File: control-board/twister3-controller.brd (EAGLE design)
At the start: 275.6 x 100 mm, 47 parts, among them IC2 TMC2130-LA, U1 MAX6816, U2 LCD-16X2SILK, U3 IS31FL3193, U4 MIC4680-5.0YM-TR

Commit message: Pretty much done with r1.0 of control board
- Stacking PCB design
- Top PCB is a panel that fits into a plastic enclosure
- Bottom holds electronics (Teensy 3.2, LCD, motor driver, encoder, etc)
- 0.1" headers hold the two boards together
- I'm trying to use hacked GND press clips to clip the LCD PCB to the
panel board instead of screws/standoffs. The goal is the two PCBs should
snap together without screws.
- I ordered the DK parts to check fits etc. I will then make final
changes and send out PCB.
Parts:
- removed CFG1, CFG2: JUMPER3-0201, we-rcl:JUMPER3-0201
- removed IC2: TMC2130-LA, we-chip:QFN36-PAD
- removed JP10, JP8, JP9: (no value), pinhead:1X01
- removed R20: 20k, we-rcl:POT_EVM3R
- removed SPI1: JUMPER2-0402-NC, we-rcl:JUMPER2-0402_NC
- removed U$1: TEENSY_3.1_ALL_PINS_AND_PADS, jonnew:TEENSY_3.1_ALLPINS
- added J10, J12, J8, J9: (no value), jonnew:1X04
- added J11, J3, J4, J5, J6: (no value), jonnew:JP4_SMD
- added J2: OSTVN04A150, jonnew:1X04
- added J7: BARREL-JACK_PJ-063BH, jonnew:PJ-063BH
- added R10: 20k, jonnew:SM-42/43W
- added R12: 4.7k, jonnew:0805
- added R14, R15: 4.7k, cyclops:0603
- added R16: 100k, jonnew:0805
- added S2: 800AWSP9M2QE, jonnew:800AWSP9M2QE
- added TP1: RESET, jonnew:TESTPOINT_1MM
- added TP2, TP3, TP4: S7121-42R, jonnew:S7121-42R
- added U10: Teensy 3.2, jonnew:TEENSY_3.1_CYCLOPS
- added U11: TMC2130-LA, we-chip:QFN36-PAD
- C12: device rcl:C0603 -> jonnew:0603
- C13, C16, C17, R22: device we-rcl:C0402 -> jonnew:0402
- C14: value 470n/10V -> 470nF/10V; device we-rcl:C0402 -> jonnew:0402
- C15: value 4u7/10V -> 47uF/10V; device we-rcl:C0402 -> jonnew:0402
- C18: value 100n/50V -> 100nF/50V; device we-rcl:C0402 -> jonnew:0402
- C19: value 22n/50V -> 22nF/50V; device we-rcl:C0402 -> jonnew:0402
- J1: device jonnew:SCREW4 -> jonnew:1X04
- R18, R19: value R0805/0R11 -> 0.11; device rcl:M0805 -> jonnew:0805
- R2: value (none) -> 20k
- R23: value 2R2 -> 2.2; device we-rcl:C0402 -> jonnew:0402
- S1: value (none) -> EC12P
- U2: value LCD-16X2SILK -> GDM1602K
- U4: device jonnew:SOP65P490X110-8N -> jonnew:SOIC127P500X400-8N
- moved C8 258.5 mm to (89.6, 34.2), flipped to the bottom, turned to 270 degrees
- moved C7 226.3 mm to (70.8, 30.2), flipped to the bottom, turned to 270 degrees
- moved D1 225.0 mm to (76.5, 34.5), flipped to the bottom, turned to 90 degrees
- moved U4 220.9 mm to (81.6, 33.3), flipped to the bottom, turned to 270 degrees
- moved L1 215.8 mm to (72.7, 44.6), flipped to the bottom, turned to 180 degrees
- moved C1 198.6 mm to (66.1, 21.6), flipped to the bottom
- moved C6 190.0 mm to (55.6, 20.0), flipped to the bottom, turned to 90 degrees
- moved C5 186.6 mm to (53.3, 20.0), flipped to the bottom, turned to 90 degrees
- moved U3 181.2 mm to (49.9, 18.1), flipped to the bottom
- moved R7 181.0 mm to (44.4, 16.2), flipped to the bottom, turned to 180 degrees
- moved R3 180.0 mm to (44.4, 18.6), flipped to the bottom, turned to 180 degrees
- moved R19 173.3 mm to (60.6, 38.7), flipped to the bottom, turned to 0 degrees
- moved JP6 170.1 mm to (53.0, 33.7), flipped to the bottom, turned to 0 degrees
- moved C16 170.1 mm to (60.4, 41.3), flipped to the bottom
- moved C12 169.5 mm to (62.1, 43.3), flipped to the bottom, turned to 90 degrees
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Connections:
- net N$5 renamed SW
- removed net !SHDN: U3.1
- removed net +5V: C15.2, IC2.25, R22.2, R23.2
- removed net AREF: U$1.AREF
- removed net CFG-0: IC2.5, JP6.4
- removed net CFG-1: IC2.4, JP6.7
- removed net CFG-2: IC2.3, JP6.6
- removed net CFG-3: IC2.2, JP6.5
- removed net MISO: U$1.12
- removed net MOSI: U$1.11
- removed net N$12: U$1.0, U2.4
- removed net N$13: U$1.1, U2.5
- removed net N$14: U$1.2, U2.6
- removed net N$15: U$1.3, U2.7
- removed net N$16: U$1.4, U2.8
- removed net N$17: U$1.5, U2.9
- removed net N$18: U$1.6, U2.10
- removed net N$19: U$1.7, U2.11
- removed net N$20: U$1.8, U2.12
- removed net N$21: U$1.9, U2.13
- removed net N$22: U$1.10, U2.14
- removed net N$30: IC2.10, SPI1.2
- removed net SCLK: U$1.13
- removed net VBAT: U$1.VBAT
- removed net VIO: C13.2, CFG1.3, CFG2.3, IC2.8, JP7.7
- removed net VUSB: U$1.VUSB
- new net !IS31_SHDN: R16.1, U10.33, U3.1
- new net +5VOUT: C15.2, R22.2, R23.2, U11.25
- new net CFG-0/MISO: JP6.4, U10.12, U11.5
- new net CFG-1/MOSI: JP6.7, U10.11, U11.4
- new net CFG-2/SCLK: JP6.6, U10.13, U11.3
- new net CFG-3/!TMC_CS: JP6.5, U10.31, U11.2
- new net DB0: U10.3, U2.7
- new net DB1: U10.4, U2.8
- new net DB2: U10.5, U2.9
- new net DB3: U10.6, U2.10
- new net DB4: U10.7, U2.11
- new net DB5: U10.8, U2.12
- new net DB6: U10.9, U2.13
- new net DB7: U10.10, U2.14
- new net E: U10.2, U2.6
- new net MECH1: J11.1, J11.2, J11.3, J11.4
- new net MECH2: J6.1, J6.2, J6.3, J6.4
- new net MECH3: J4.1, J4.2, J4.3, J4.4, TP2.P$1
- new net MECH4: J5.1, J5.2, J5.3, J5.4, TP3.P$1, TP4.P$1
- new net N$23: S2.1, TP1.1
- new net N$6: J2.1, J3.4
- new net N$7: J2.2, J3.3
- new net N$8: J2.3, J3.2
- new net N$9: J2.4, J3.1
- new net RS: U10.0, U2.4
- new net RW: U10.1, U2.5
- new net SD_MODE: U10.16/A2, U11.9
- new net SPI_MODE: U10.15/A1, U11.10
- net +24V0: now also J7.1, U11.16, U11.30, U11.31; no longer IC2.16, IC2.30, IC2.31
- net +3V3: now also C13.2, JP7.7, U10.3.3V, U10.3.3V2, U11.8; no longer R1.2, R2.1, R3.1, R6.2, R7.1, U$1.3.3V, U$1.3.3V1, U$1.3.3V2, U2.15, U2.2
- net +5V0: now also R1.2, R12.2, R14.2, R15.2, R2.1, R3.1, R6.2, R7.1, U10.VIN, U2.15, U2.2; no longer U$1.VIN
- net AGND: now also U10.AGND; no longer U$1.AGND
- net BRA1: now also U11.33; no longer IC2.33
- net BRB1: now also U11.14; no longer IC2.14
- net BUTT: now also U10.21/A7; no longer U$1.16/A2
- net CFG-6: now also U10.26, U11.22; no longer IC2.22
- net CFG4: now also U10.14/A0, U11.18; no longer CFG1.2, IC2.18
- net CFG5: now also U10.30, U11.19; no longer CFG2.2, IC2.19
- net CPI1: now also U11.28; no longer IC2.28
- net CPO1: now also U11.27; no longer IC2.27
- net DIAG0: now also R15.1, U10.29, U11.20; no longer IC2.20, JP8.1
- net DIAG1: now also R14.1, U10.28, U11.21; no longer IC2.21, JP9.1
- net DIR: now also U10.17/A3, U11.7; no longer IC2.7, U$1.21/A7
- net ENC_A: now also U10.22/A8; no longer U$1.14/A0
- net ENC_B: now also U10.23/A9; no longer U$1.15/A1
- net GND: now also J7.2, R10.3, R16.2, S2.2, U10.GND, U10.GND2, U11.1, U11.11, U11.12, U11.24, U11.35, U11.36, U11.TP; no longer CFG1.1, CFG2.1, IC2.1, IC2.11, IC2.12, IC2.24, IC2.35, IC2.36, IC2.TP, R20.3, SPI1.1, U$1.GND, U$1.GND1, U$1.GND2
- net IREF: now also R10.2, U11.23; no longer IC2.23, JP10.1, R20.2
- net OA1: now also U11.34; no longer IC2.34
- net OA2: now also U11.32; no longer IC2.32
- net OB1: now also U11.13; no longer IC2.13
- net OB2: now also U11.15; no longer IC2.15
- net SCL: now also U10.19/A5; no longer U$1.19/A5
- net SDA: now also U10.18/A4; no longer U$1.18/A4
- net STEP: now also U10.32, U11.6; no longer IC2.6, U$1.20/A6
- net VCC1: now also U11.26; no longer IC2.26
- net VCP1: now also U11.29; no longer IC2.29
- net VREF2: now also R10.1; no longer R20.1
- net V_BM: now also R12.1
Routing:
- net +3V3: track 0.00 -> 86.4 mm, vias 0 -> 1
- net RS: track 0.00 -> 60.0 mm
- net RW: track 0.00 -> 57.4 mm
- net E: track 0.00 -> 55.7 mm
- net DB0: track 0.00 -> 54.1 mm
- net DB1: track 0.00 -> 52.4 mm
- net DB2: track 0.00 -> 50.7 mm
- net DB3: track 0.00 -> 49.1 mm
- net DB4: track 0.00 -> 47.4 mm
- net DB5: track 0.00 -> 45.8 mm
- net DB6: track 0.00 -> 44.1 mm
- net DB7: track 0.00 -> 42.3 mm
- net CFG-0/MISO: track 0.00 -> 40.6 mm, vias 0 -> 1
- net +5VOUT: track 0.00 -> 40.2 mm
- net CFG-1/MOSI: track 0.00 -> 39.7 mm, vias 0 -> 2
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- added copper zone on layer 16, net +24V0
- added copper zone on layer 15, net +3V3
- added copper zone on layer 16, net +5V0
- added copper zone on layer 2, net +5V0
- added copper zone on layer 16, net MECH1
- added copper zone on layer 16, net MECH2
- added copper zone on layer 16, net MECH3
- added copper zone on layer 16, net MECH4
- added copper zone on layer 1, net SW
- added copper zone on layer 16, net SW
- removed copper zone on layer 1, net +24V0
- removed copper zone on layer 15, net VIO
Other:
- board size 275.6 x 100 mm -> 191 x 90.5 mm
- board text added: "- Teensy goes on bottom with top of board facing up. - Silent stepper stick goes on bottom with top of board facing down - Inner holes are for 1/2" standoffs"
- board text added: "0.5" standoffs"
- board text added: "SilentStepStick Compatible"
- board text added: "Top Board Origin"
- board text added: "Twister 3 Control Board CERN OHL v1.2 Jon Newman MIT 2018"
- board text added: "V-CUT"
- board text removed: "SilentStepStick"
- board text removed: "TOP"
- board text removed: "www.watterott.com"

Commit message: Complete rev 1.0 of control board
- Off to fab
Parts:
- U2: device SparkFun-Displays:LCD-16X2 -> jonnew:LCD-16X2
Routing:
- net RS: track 60.0 -> 63.7 mm
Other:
- board text added: "- Board to panel stack height: 12 mm. - Teensy goes on bottom with top of teensy facing up (when board is flipped) - Silent stepper stick goes on bottom with top of module facing down (whe board flipped)"
- board text added: "M1"
- board text added: "M2"
- board text added: "M3"
- board text added: "M4"
- board text added: "M5"
- board text removed: "- Teensy goes on bottom with top of board facing up. - Silent stepper stick goes on bottom with top of board facing down - Inner holes are for 1/2" standoffs"
- board text removed: "0.5" standoffs"
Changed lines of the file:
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@@
 <setting verticaltext="up"/>
 </settings>
-<grid distance="0.001429" unitdist="inch" unit="inch" style="lines" multiple="1" display="yes" altdistance="5" altunitdist="mil" altunit="mil"/>
+<grid distance="0.5" unitdist="mm" unit="mm" style="lines" multiple="1" display="yes" altdistance="5" altunitdist="mil" altunit="mil"/>
 <layers>
 <layer number="1" name="Top" color="4" fill="1" visible="yes" active="yes"/>
@@
 <layer number="37" name="tTest" color="7" fill="1" visible="no" active="yes"/>
 <layer number="38" name="bTest" color="7" fill="1" visible="no" active="yes"/>
-<layer number="39" name="tKeepout" color="4" fill="11" visible="no" active="yes"/>
+<layer number="39" name="tKeepout" color="4" fill="11" visible="yes" active="yes"/>
 <layer number="40" name="bKeepout" color="1" fill="11" visible="no" active="yes"/>
 <layer number="41" name="tRestrict" color="4" fill="10" visible="no" active="yes"/>
 <layer number="42" name="bRestrict" color="1" fill="10" visible="no" active="yes"/>
 <layer number="43" name="vRestrict" color="2" fill="10" visible="no" active="yes"/>
-<layer number="44" name="Drills" color="7" fill="1" visible="no" active="yes"/>
-<layer number="45" name="Holes" color="7" fill="1" visible="no" active="yes"/>
+<layer number="44" name="Drills" color="7" fill="1" visible="yes" active="yes"/>
+<layer number="45" name="Holes" color="7" fill="1" visible="yes" active="yes"/>
 <layer number="46" name="Milling" color="3" fill="1" visible="no" active="yes"/>
 <layer number="47" name="Measures" color="7" fill="1" visible="no" active="yes"/>
@@
 <layer number="49" name="Reference" color="7" fill="1" visible="no" active="yes"/>
 <layer number="50" name="dxf" color="7" fill="1" visible="no" active="no"/>
-<layer number="51" name="tDocu" color="7" fill="1" visible="no" active="yes"/>
+<layer number="51" name="tDocu" color="7" fill="1" visible="yes" active="yes"/>
 <layer number="52" name="bDocu" color="7" fill="1" visible="no" active="yes"/>
 <layer number="53" name="tGND_GNDA" color="7" fill="9" visible="no" active="no"/>
@@
 <hole x="187.8" y="63.39" drill="3"/>
 <hole x="187.8" y="3.85" drill="3"/>
-<text x="-7" y="-4.1" size="1.016" layer="51" rot="R180">0.5" standoffs</text>
 <wire x1="95.5" y1="1" x2="95.5" y2="-1" width="0.127" layer="51"/>
 <wire x1="94.5" y1="0" x2="96.5" y2="0" width="0.127" layer="51"/>
-<text x="95.5" y="-3" size="1.016" layer="51">Top Board Origin</text>
+<text x="96.5" y="-2" size="1.016" layer="51">Top Board Origin</text>
 <wire x1="0.5" y1="51" x2="0.5" y2="16" width="0" layer="20"/>
 <wire x1="0.5" y1="16" x2="16" y2="0.5" width="0" layer="20"/>
@@
 <wire x1="108.5" y1="27.5" x2="178.5" y2="27.5" width="0" layer="20"/>
 <wire x1="179.5" y1="28.5" x2="179.5" y2="53.5" width="0" layer="20"/>
-<text x="18.1" y="-23.2" size="1.016" layer="51">- Teensy goes on bottom with top of board facing up.
-- Silent stepper stick goes on bottom with top of board facing down
-- Inner holes are for 1/2" standoffs</text>
 <circle x="160.5" y="12" radius="4.75" width="0.05" layer="20"/>
 <wire x1="178.5" y1="54.5" x2="108.5" y2="54.5" width="0" layer="20"/>
-<wire x1="-6.5" y1="-4" x2="10" y2="10.4" width="0.01" layer="51"/>
 <wire x1="107.5" y1="53.5" x2="108.5" y2="54.5" width="0" layer="20" curve="-233.130102"/>
 <wire x1="108.5" y1="27.5" x2="107.5" y2="28.5" width="0" layer="20" curve="-233.130102"/>
@@
 <rectangle x1="127.2643875" y1="60.579" x2="127.59204375" y2="60.61506875" layer="21"/>
 <rectangle x1="113.728728125" y1="60.61506875" x2="113.982728125" y2="60.6513875" layer="21"/>
+<hole x="85" y="46.5" drill="3"/>
+<hole x="6.5" y="48" drill="3"/>
+<hole x="6" y="19" drill="3"/>
+<circle x="85" y="46.5" radius="3.5" width="0" layer="39"/>
+<circle x="6.5" y="48" radius="3.5" width="0" layer="39"/>
+<circle x="6" y="19" radius="3.5" width="0" layer="39"/>
+<circle x="78" y="13.5" radius="3.5" width="0" layer="39"/>
+<hole x="78" y="13.5" drill="3"/>
+<circle x="45.5" y="63" radius="3.5" width="0" layer="39"/>
+<hole x="45.5" y="63" drill="3"/>
+<text x="4" y="21.5" size="1.27" layer="21" font="vector" ratio="18">M1</text>
+<text x="5" y="50.5" size="1.27" layer="21" font="vector" ratio="18">M2</text>
+<text x="41" y="62.5" size="1.27" layer="21" font="vector" ratio="18">M3</text>
+<text x="84" y="48.5" size="1.27" layer="21" font="vector" ratio="18">M4</text>
+<text x="77" y="16" size="1.27" layer="21" font="vector" ratio="18">M5</text>
+<text x="17.5" y="77" size="1.27" layer="51" font="vector" ratio="18">- Board to panel stack height:  12 mm.
+- Teensy goes on bottom with top of teensy facing up (when board is flipped)
+- Silent stepper stick goes on bottom with top of module facing down (whe board flipped)</text>
 </plain>
 <attributes>
@@
 <attribute name="VALUE" x="49.54" y="11.25" size="1.016" layer="28" font="vector" ratio="19" rot="MR0"/>
 </element>
-<element name="U2" library="SparkFun-Displays" package="LCD-16X2" value="GDM1602K" x="48" y="41" smashed="yes">
+<element name="U2" library="jonnew" package="LCD-16X2" value="GDM1602K" x="48" y="41" smashed="yes">
 <attribute name="NAME" x="8.6" y="21.7" size="1.016" layer="25" font="vector" ratio="19"/>
 <attribute name="SF_ID" value="LCD-00255" x="48" y="41" size="1.778" layer="27" display="off"/>
@@
 <attribute name="DK" value="" x="55.6" y="20" size="1.778" layer="28" rot="MR90" display="off"/>
 <attribute name="MN" value="TDK Corp." x="55.6" y="20" size="1.778" layer="28" rot="MR90" display="off"/>
-<attribute name="NAME" x="57.04" y="22.75" size="1.016" layer="26" font="vector" ratio="19" rot="MR90"/>
+<attribute name="NAME" x="58.54" y="19.75" size="1.016" layer="26" font="vector" ratio="19" rot="MR90"/>
 <attribute name="PARTNO" value="C2012X5R1Cxxxxxxx" x="55.6" y="20" size="1.778" layer="28" rot="MR90" display="off"/>
-<attribute name="VALUE" x="55.79" y="22.75" size="1.016" layer="28" font="vector" ratio="19" rot="MR90"/>
+<attribute name="VALUE" x="57.29" y="19.75" size="1.016" layer="28" font="vector" ratio="19" rot="MR90"/>
 <attribute name="VID" value="DK" x="55.6" y="20" size="1.778" layer="28" rot="MR90" display="off"/>
 </element>
@@
 </element>
 <element name="C7" library="jonnew" package="7343M" value="T491D227M010AT" x="70.838" y="30.206" smashed="yes" rot="MR270">
-<attribute name="NAME" x="65.54" y="23.75" size="1.016" layer="26" font="vector" ratio="19" rot="MR90"/>
-<attribute name="VALUE" x="64.29" y="23.75" size="1.016" layer="28" font="vector" ratio="19" rot="MR90"/>
+<attribute name="NAME" x="66.25" y="31.46" size="1.016" layer="25" font="vector" ratio="19" rot="R180"/>
+<attribute name="VALUE" x="66.25" y="30.21" size="1.016" layer="27" font="vector" ratio="19" rot="R180"/>
 </element>
 <element name="C8" library="jonnew" package="7343M" value="T491D156K035AT" x="89.648" y="34.22" smashed="yes" rot="MR270">
@@
 <wire x1="38.35" y1="8.35" x2="40.5" y2="10.5" width="1" layer="1"/>
 <wire x1="40.5" y1="10.5" x2="40.5" y2="23" width="1" layer="1"/>
-<wire x1="40.5" y1="23" x2="45.25" y2="27.75" width="1" layer="1"/>
-<wire x1="45.25" y1="27.75" x2="60.25" y2="27.75" width="1" layer="1"/>
-<wire x1="60.25" y1="27.75" x2="64.5" y2="32" width="1" layer="1"/>
+<wire x1="60.75" y1="28.25" x2="64.5" y2="32" width="1" layer="1"/>
 <wire x1="60.5" y1="48.5" x2="63.5" y2="48.5" width="1" layer="1"/>
 <wire x1="63.5" y1="48.5" x2="64.5" y2="47.5" width="1" layer="1"/>
@@
 <wire x1="34.9" y1="19.8" x2="34.9" y2="17.95" width="1" layer="16"/>
 <wire x1="34.9" y1="17.95" x2="33.5" y2="16.55" width="1" layer="16"/>
+<wire x1="45.75" y1="28.25" x2="60.75" y2="28.25" width="1" layer="1"/>
+<wire x1="40.5" y1="23" x2="45.75" y2="28.25" width="1" layer="1"/>
 </signal>
 <signal name="N$4">
@@
 <contactref element="U2" pad="4"/>
 <contactref element="U10" pad="0"/>
-<wire x1="12.4" y1="24.71299375" x2="12.4" y2="26.28700625" width="0.2" layer="1"/>
-<wire x1="12.4" y1="26.28700625" x2="12" y2="26.68700625" width="0.2" layer="1"/>
-<wire x1="12.3" y1="24.61299375" x2="12.4" y2="24.71299375" width="0.2" layer="1"/>
-<wire x1="12.3" y1="16.19" x2="12.3" y2="24.61299375" width="0.2" layer="1"/>
 <wire x1="23.62" y1="55.62" x2="12" y2="44" width="0.2" layer="1"/>
-<wire x1="12" y1="26.68700625" x2="12" y2="44" width="0.2" layer="1"/>
-<wire x1="22.68" y1="5.81" x2="12.3" y2="16.19" width="0.2" layer="1"/>
+<wire x1="12" y1="44" x2="12" y2="32" width="0.2" layer="1"/>
 <wire x1="23.62" y1="56.5" x2="23.62" y2="55.62" width="0.2" layer="1"/>
+<wire x1="12" y1="19.5" x2="12" y2="16.49" width="0.2" layer="1"/>
+<wire x1="12" y1="16.49" x2="22.68" y2="5.81" width="0.2" layer="1"/>
+<wire x1="12" y1="32" x2="7.5" y2="27.5" width="0.2" layer="1"/>
+<wire x1="7.5" y1="27.5" x2="7.5" y2="24" width="0.2" layer="1"/>
+<wire x1="7.5" y1="24" x2="12" y2="19.5" width="0.2" layer="1"/>
 </signal>
 <signal name="RW">
@@
 <vertex x="68" y="58"/>
 <vertex x="68" y="52"/>
-<vertex x="85" y="52"/>
-<vertex x="85" y="41"/>
+<vertex x="83.3" y="52"/>
+<vertex x="83.3" y="41"/>
 <vertex x="80.9" y="41"/>
 <vertex x="80.9" y="37.5"/>

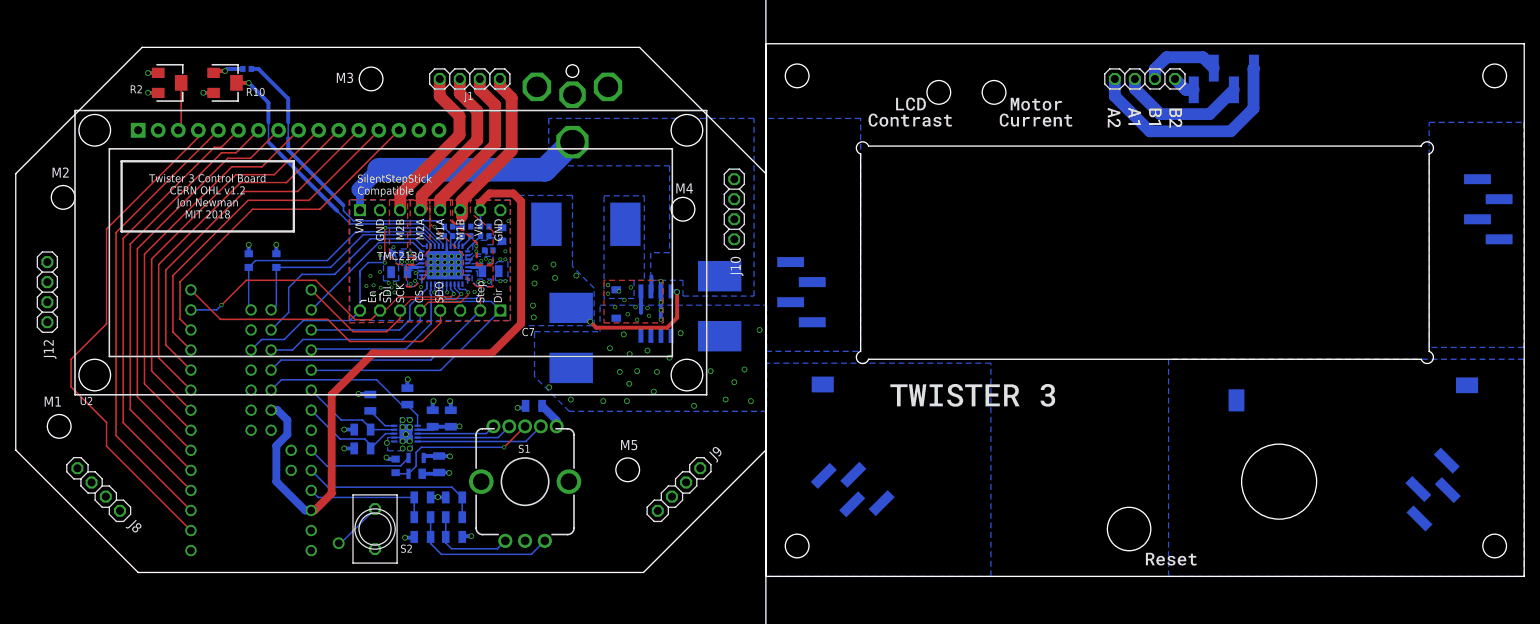
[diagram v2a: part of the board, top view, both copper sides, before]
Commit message: Updated control board after assembly
- Removed redudant mechanical connectors
- Added positions for SMD nuts on bottom of panel board
- Replace most 0805 components with 0603
- Other minor changes
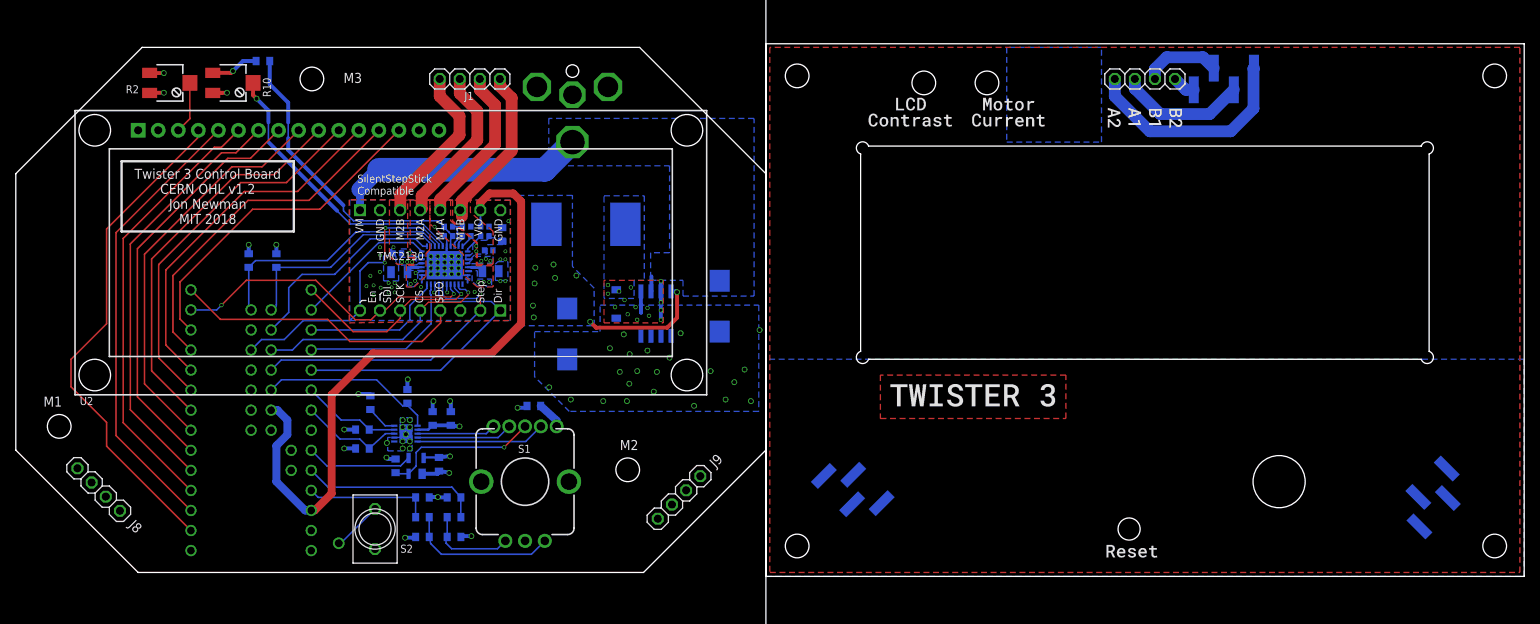
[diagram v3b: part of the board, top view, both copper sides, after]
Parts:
- removed J10, J12: (no value), jonnew:1X04
- removed J11, J6: (no value), jonnew:JP4_SMD
- removed TP2, TP3, TP4: S7121-42R, jonnew:S7121-42R
- C1, C2, C3, C4, C5, C6, R1, R12, R16, R3, R4, R5, R6, R7: device jonnew:0805 -> jonnew:0603
- R10, R2: device jonnew:SM-42/43W -> jonnew:SM-42/43X
- R22: device jonnew:0402 -> jonnew:0603
- moved R22 2.24 mm to (31.8, 65.3)
- moved J5 1.00 mm to (180.0, 10.0)
- moved J9 1.00 mm to (84.5, 10.0)
- moved R10 1.00 mm to (28.0, 62.5)
- moved C7 0.71 mm to (70.3, 30.7)
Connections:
- removed net MECH1: J11.1, J11.2, J11.3, J11.4
- removed net MECH2: J6.1, J6.2, J6.3, J6.4
- removed net MECH3: J4.1, J4.2, J4.3, J4.4, TP2.P$1
- removed net MECH4: J5.1, J5.2, J5.3, J5.4, TP3.P$1, TP4.P$1
- new net MECH: J4.1, J4.2, J4.3, J4.4, J5.1, J5.2, J5.3, J5.4
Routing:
- net GND: track 24.3 -> 28.1 mm
- net IREF: track 38.2 -> 36.4 mm
- net VREF2: track 4.38 -> 6.10 mm
- net +5V0: track 38.9 -> 40.2 mm
- net N$11: track 6.15 -> 7.13 mm
- net CFG-6: track 37.5 -> 36.8 mm
- added copper zone on layer 16, net MECH
- added copper zone on layer 16, net N$12
- added copper zone on layer 1, net N$13
- added copper zone on layer 1, net N$5
- removed copper zone on layer 16, net MECH1
- removed copper zone on layer 16, net MECH2
- removed copper zone on layer 16, net MECH3
- removed copper zone on layer 16, net MECH4
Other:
- outline, holes or cut-outs redrawn
- board text added: "M6"
- board text removed: "CS/CFG3"
- board text removed: "DIAG0"
- board text removed: "DIAG1"
- board text removed: "En/CFG6"
- board text removed: "Motor Coil 1-A"
- board text removed: "Motor Coil 1-B"
- board text removed: "Motor Coil 2-A"
- board text removed: "Motor Coil 2-B"
- board text removed: "SCK/CFG2"
- board text removed: "SDI/CFG1"
- board text removed: "SDO/CFG0"
- board text removed: "Silkscreen: 22 bPlace"
- board text removed: "VRef"
- board text removed: "Vio - 3.3-5V"
- board text removed: "Vm"
- board text removed: "nc"
